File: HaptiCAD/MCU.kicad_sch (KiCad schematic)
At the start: 16 parts, among them J801 SWD, J802 Micro_SD_Card, U801 BMD-340-A-R, U802 ESD224DQA

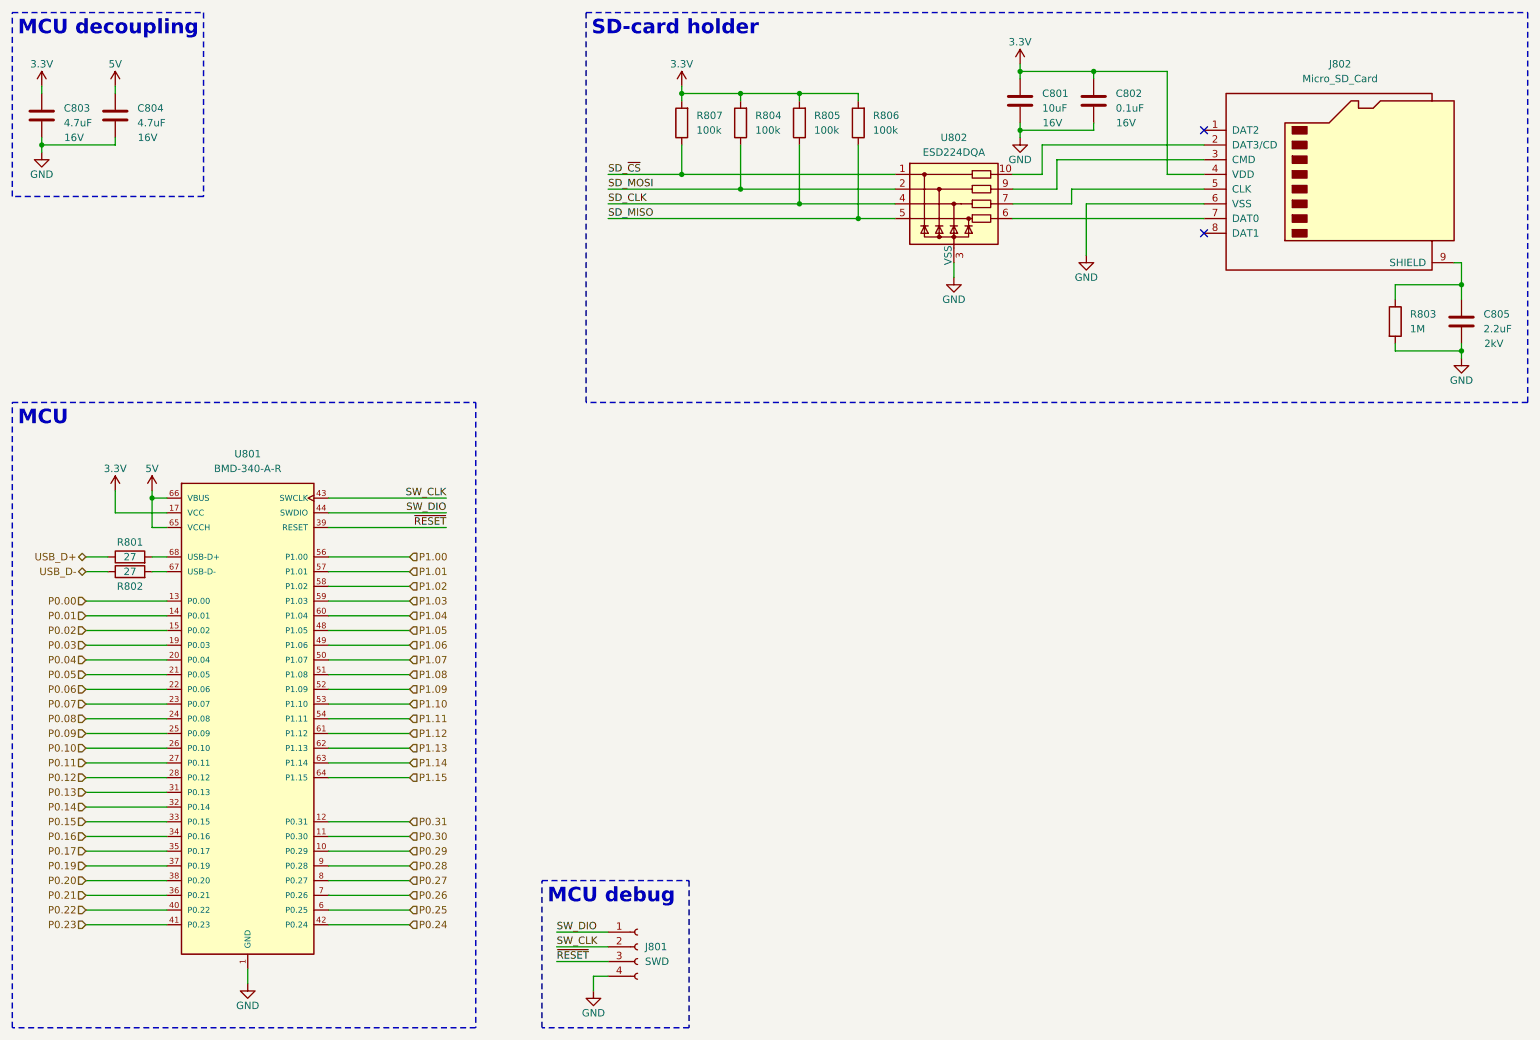
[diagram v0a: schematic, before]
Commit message: Updated name, schematic and pcb
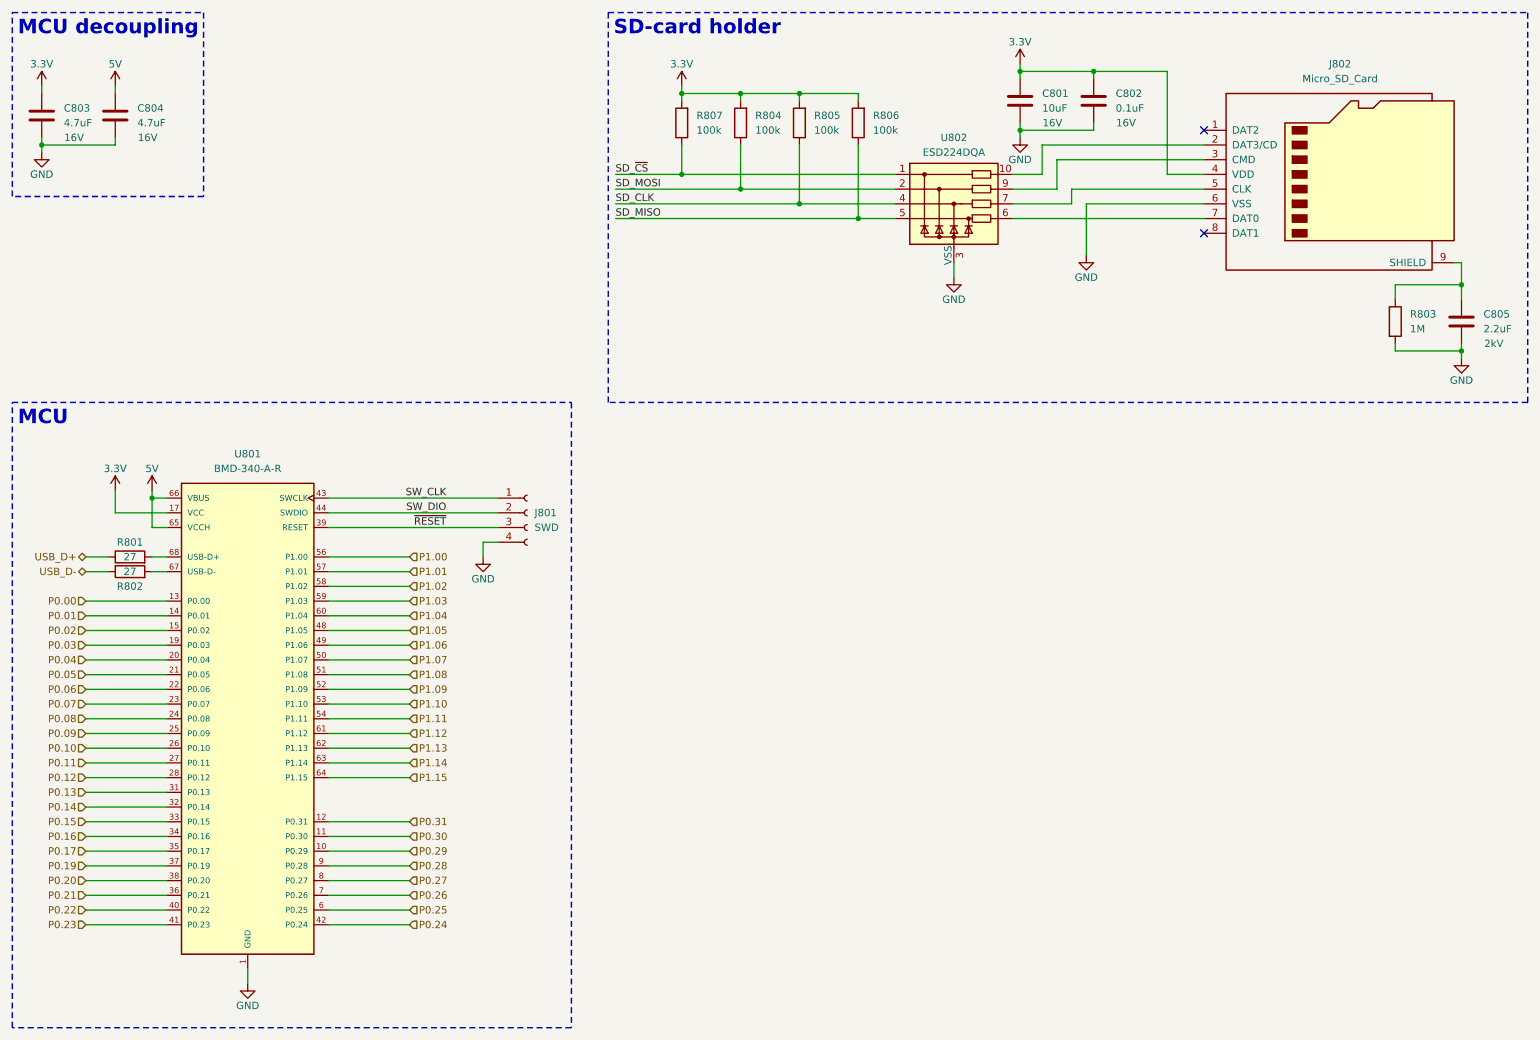
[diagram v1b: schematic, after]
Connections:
- net SW_CLK: now also J801.1 (Pin_1); no longer J801.2 (Pin_2)
- net SW_DIO: now also J801.2 (Pin_2); no longer J801.1 (Pin_1)
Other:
- moved on the sheet: J801
